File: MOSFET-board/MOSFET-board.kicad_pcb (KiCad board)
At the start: 2 copper layers, 76.2 x 76.2 mm, 104 parts, among them J1 PCIE-LP-01-01-F-DV-A-TR, J2 DB25_Female, U1 BTS3080EJXUMA1, U10 BTS3080EJXUMA1, U11 PCF8575_Breakout, U2 BTS3080EJXUMA1, U3 BTS3080EJXUMA1, U4 BTS3080EJXUMA1, U5 BTS3080EJXUMA1, U6 BTS3080EJXUMA1, U7 BTS3080EJXUMA1, U8 BTS3080EJXUMA1, U9 BTS3080EJXUMA1

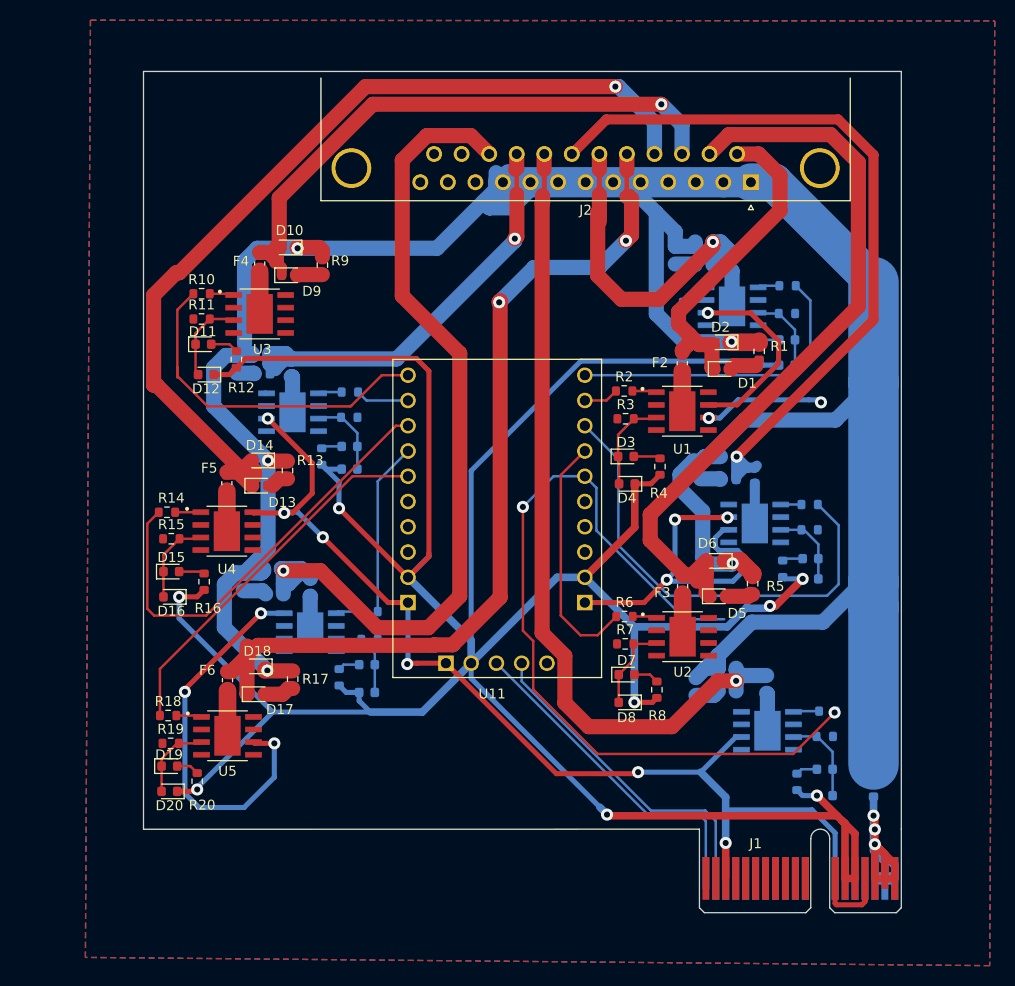
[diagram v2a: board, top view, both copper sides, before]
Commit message: Finished mosfet layout
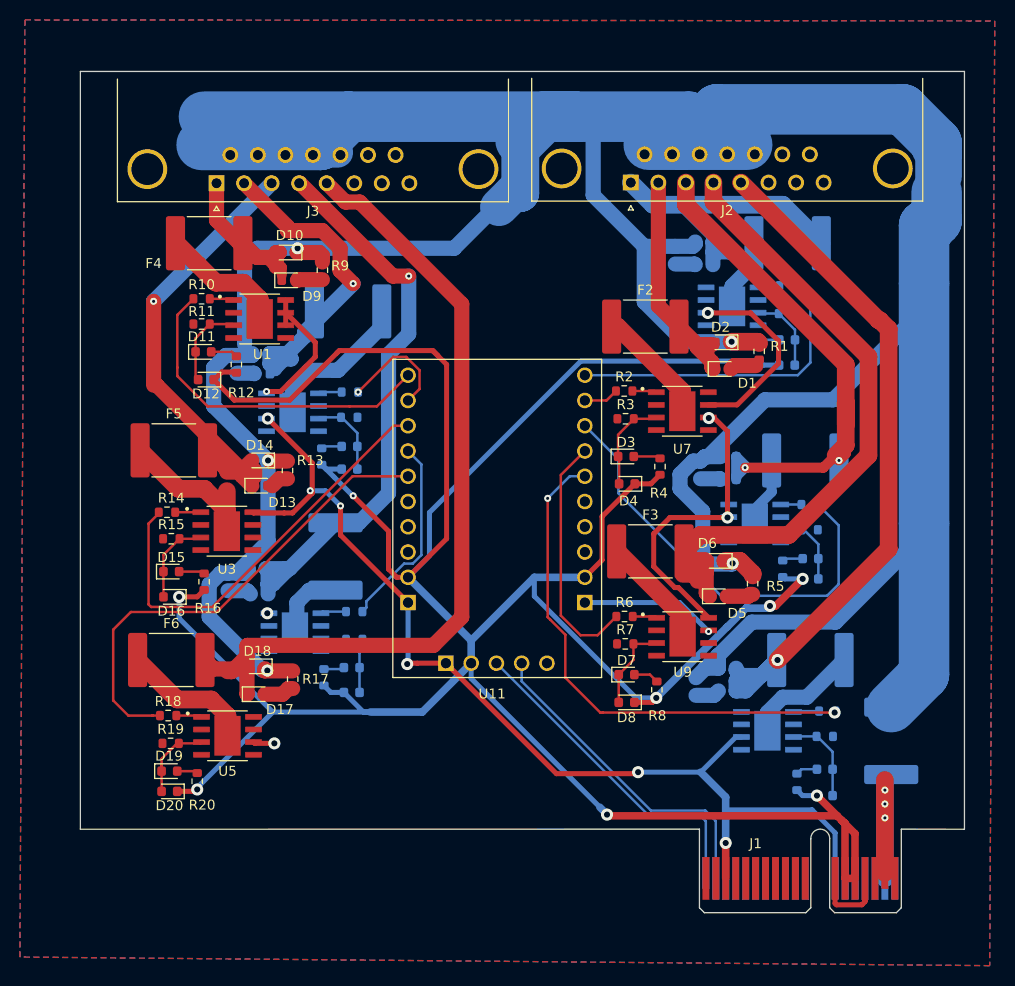
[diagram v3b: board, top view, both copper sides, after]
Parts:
- added J3: DB15_Female, Connector_Dsub:DSUB-15_Female_Horizontal_P2.77x2.84mm_EdgePinOffset7.70mm_Housed_MountingHolesOffset9.12mm, F.Cu at (134.3, 74.7)
- F1, F10, F11, F2, F3, F4, F5, F6, F7, F8, F9: footprint Fuse:Fuse_0603_1608Metric -> Fuse:Fuse_2920_7451Metric
- J2: value DB25_Female -> DB15_Female; footprint Connector_Dsub:DSUB-25_Male_Horizontal_P2.77x2.84mm_EdgePinOffset7.70mm_Housed_MountingHolesOffset9.12mm -> Connector_Dsub:DSUB-15_Female_Horizontal_P2.77x2.84mm_EdgePinOffset7.70mm_Housed_MountingHolesOffset9.12mm
- moved J2 12.1 mm to (176.0, 74.7)
- moved F10 7.99 mm to (147.6, 87.6), turned to 180 degrees
- moved F5 6.27 mm to (130.0, 101.6), turned to 0 degrees
- moved F6 6.01 mm to (129.8, 122.7), turned to 0 degrees
- moved F7 5.92 mm to (191.8, 80.8), turned to 0 degrees
- moved F4 5.47 mm to (133.6, 80.8), turned to 0 degrees
- moved F8 5.30 mm to (193.5, 102.6), turned to 0 degrees
- moved F2 5.23 mm to (177.5, 89.2), turned to 0 degrees
- moved F1 5.14 mm to (202.2, 130.8)
- moved F9 4.98 mm to (194.1, 122.7), turned to 180 degrees
- moved F3 4.77 mm to (178.0, 111.8), turned to 0 degrees
- moved F11 3.93 mm to (146.3, 112.3)
- moved D39 1.56 mm to (147.9, 123.4)
- moved D37 1.54 mm to (138.5, 116.0)
- moved D38 1.54 mm to (138.5, 113.5)
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- renumbered U3 to U1, U8 to U10, U9 to U2, U4 to U3, U10 to U4, U1 to U7, U7 to U8, U2 to U9
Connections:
- D1 pad 1: PYRO1 -> PYRO7
- D10 pad 2: PYRO3 -> PYRO1
- D13 pad 1: PYRO4 -> PYRO3
- D14 pad 2: PYRO4 -> PYRO3
- D2 pad 2: PYRO1 -> PYRO7
- D25 pad 1: PYRO7 -> PYRO8
- D26 pad 2: PYRO7 -> PYRO8
- D29 pad 1: PYRO8 -> PYRO10
- D30 pad 2: PYRO8 -> PYRO10
- D33 pad 1: PYRO9 -> PYRO2
- D34 pad 2: PYRO9 -> PYRO2
- D37 pad 1: PYRO10 -> PYRO4
- D38 pad 2: PYRO10 -> PYRO4
- D5 pad 1: PYRO2 -> PYRO9
- D6 pad 2: PYRO2 -> PYRO9
- D9 pad 1: PYRO3 -> PYRO1
- F10 pad 2: PYRO9 -> PYRO2
- F11 pad 2: PYRO10 -> PYRO4
- F2 pad 2: PYRO1 -> PYRO7
- F3 pad 2: PYRO2 -> PYRO9
- F4 pad 2: PYRO3 -> PYRO1
- F5 pad 2: PYRO4 -> PYRO3
- F8 pad 2: PYRO7 -> PYRO8
- F9 pad 2: PYRO8 -> PYRO10
- J2 pad 1: +12V -> PYRO6
- J2 pad 11: unconnected-(J2-Pad11) -> +12V
- J2 pad 12: unconnected-(J2-Pad12) -> +12V
- J2 pad 13: unconnected-(J2-Pad13) -> +12V
- J2 pad 14: PYRO1 -> unconnected-(J2-Pad14)
- J2 pad 15: PYRO2 -> unconnected-(J2-Pad15)
- J2 pad 2: +12V -> PYRO7
- J2 pad 3: +12V -> PYRO8
- J2 pad 4: +12V -> PYRO9
- J2 pad 5: +12V -> PYRO10
- J2 pad 6: +12V -> unconnected-(J2-Pad6)
- J2 pad 7: +12V -> unconnected-(J2-Pad7)
- J2 pad 8: +12V -> unconnected-(J2-Pad8)
- R10 pad 1: PYRO3EN -> PYRO1EN
- R11 pad 1: /Pyro 3/Status -> /Pyro 1/Status
- R14 pad 1: PYRO4EN -> PYRO3EN
- R15 pad 1: /Pyro 4/Status -> /Pyro 3/Status
- R2 pad 1: PYRO1EN -> PYRO7EN
- R26 pad 1: PYRO7EN -> PYRO8EN
- R27 pad 1: /Pyro 7/Status -> /Pyro 8/Status
- R3 pad 1: /Pyro 1/Status -> /Pyro 7/Status
- R30 pad 1: PYRO8EN -> PYRO10EN
- R31 pad 1: /Pyro 8/Status -> /Pyro 10/Status
- R34 pad 1: PYRO9EN -> PYRO2EN
- R35 pad 1: /Pyro 9/Status -> /Pyro 2/Status
- R38 pad 1: PYRO10EN -> PYRO4EN
- R39 pad 1: /Pyro 10/Status -> /Pyro 4/Status
- R6 pad 1: PYRO2EN -> PYRO9EN
- R7 pad 1: /Pyro 2/Status -> /Pyro 9/Status
- U11 pad 1: PYRO3EN -> PYRO1EN
- U11 pad 2: PYRO9EN -> PYRO2EN
- U11 pad 21: PYRO8EN -> PYRO10EN
- U11 pad 22: PYRO2EN -> PYRO9EN
- U11 pad 23: PYRO7EN -> PYRO8EN
- U11 pad 24: PYRO1EN -> PYRO7EN
- U11 pad 3: PYRO4EN -> PYRO3EN
- U11 pad 4: PYRO10EN -> PYRO4EN
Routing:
- net +12V: track 296.7 -> 397.4 mm
- net PYRO7: track 75.7 -> 24.7 mm, vias 1 -> 0
- net PYRO7EN: track 47.0 -> 3.53 mm
- net PYRO2: track 76.2 -> 35.4 mm, vias 0 -> 1
- net PYRO8EN: track 83.7 -> 44.0 mm, vias 2 -> 0
- net PYRO10EN: track 17.4 -> 52.1 mm, vias 0 -> 2
- net PYRO4: track 92.8 -> 58.2 mm
- net PYRO1EN: track 3.53 -> 34.2 mm
- net GND: track 226.0 -> 197.6 mm, vias 15 -> 13
- net PYRO8: track 83.9 -> 57.0 mm, vias 1 -> 2
- net PYRO4EN: track 44.6 -> 19.7 mm
- net PYRO9: track 44.7 -> 66.9 mm, vias 1 -> 0
- net PYRO9EN: track 5.37 -> 24.7 mm
- net PYRO1: track 33.2 -> 17.1 mm
- net PYRO10: track 86.8 -> 71.1 mm
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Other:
- board size 76.2 x 76.2 mm -> 88.9 x 76.2 mm

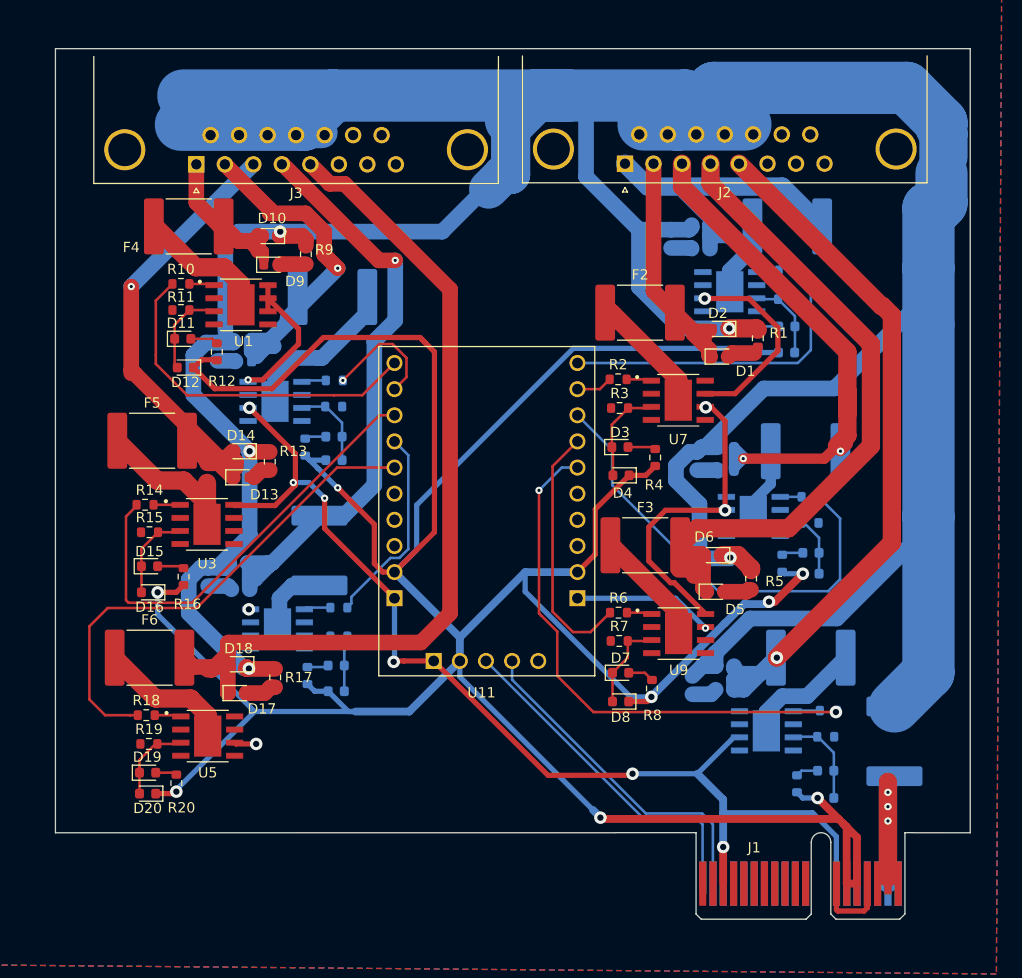
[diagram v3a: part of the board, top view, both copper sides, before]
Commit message: MOSFET Board Updated
MOSFET Board changes, new PCB Design and updated schematic.
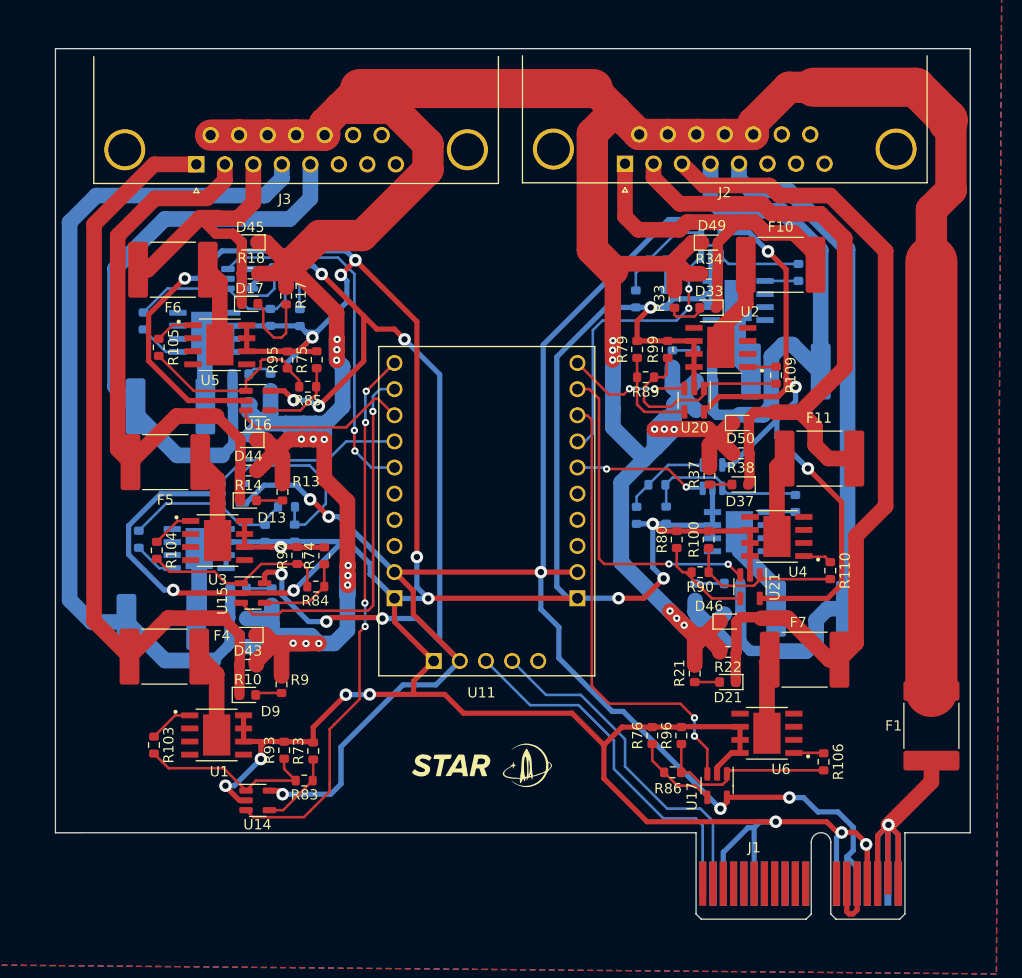
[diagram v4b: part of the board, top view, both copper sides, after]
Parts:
- removed D10, D12, D14, D16, D18, D2, D20, D22, D24, D26, D28, D30, D32, D34, D36, D38, D4, D40, D6, D8: D_Schottky, Diode_SMD:D_0603_1608Metric
- removed D11, D15, D19, D23, D27, D3, D31, D35, D39, D7: R_LED, LED_SMD:LED_0603_1608Metric
- removed R11, R15, R19, R23, R27, R3, R31, R35, R39, R7: 2k, Resistor_SMD:R_0603_1608Metric
- removed R12, R16, R20, R24, R28, R32, R36, R4, R40, R8: 3k, Resistor_SMD:R_0603_1608Metric
- added D41: D_Schottky, Diode_SMD:D_0603_1608Metric, B.Cu at (138.1, 121.6)
- added D42: D_Schottky, Diode_SMD:D_0603_1608Metric, B.Cu at (138.8, 101.0)
- added D43: D_Schottky, Diode_SMD:D_0603_1608Metric, F.Cu at (139.3, 120.5)
- added D44: D_Schottky, Diode_SMD:D_0603_1608Metric, F.Cu at (139.4, 101.5)
- added D45: D_Schottky, Diode_SMD:D_0603_1608Metric, F.Cu at (139.5, 82.3)
- added D46: D_Schottky, Diode_SMD:D_0603_1608Metric, F.Cu at (186.0, 119.2)
- added D47: D_Schottky, Diode_SMD:D_0603_1608Metric, B.Cu at (183.7, 98.6)
- added D48: D_Schottky, Diode_SMD:D_0603_1608Metric, B.Cu at (186.5, 121.1)
- added D49: D_Schottky, Diode_SMD:D_0603_1608Metric, F.Cu at (184.2, 82.3)
- added D50: D_Schottky, Diode_SMD:D_0603_1608Metric, F.Cu at (187.2, 99.9)
- added G***: LOGO, Symbol:STARLogo, F.Cu at (161.7, 133.1)
- added R100: 10k, Resistor_SMD:R_0603_1608Metric, F.Cu at (184.1, 111.2)
- added R101: 2k, Resistor_SMD:R_0603_1608Metric, B.Cu at (128.8, 111.2)
- added R102: 2k, Resistor_SMD:R_0603_1608Metric, B.Cu at (129.2, 90.0)
- added R103: 2k, Resistor_SMD:R_0603_1608Metric, F.Cu at (130.2, 131.2)
- added R104: 2k, Resistor_SMD:R_0603_1608Metric, F.Cu at (130.5, 112.2)
- added R105: 2k, Resistor_SMD:R_0603_1608Metric, F.Cu at (130.7, 92.5)
- added R106: 2k, Resistor_SMD:R_0603_1608Metric, F.Cu at (195.3, 132.8)
- added R107: 2k, Resistor_SMD:R_0603_1608Metric, B.Cu at (192.9, 85.2)
- added R108: 2k, Resistor_SMD:R_0603_1608Metric, B.Cu at (192.6, 107.7)
- added R109: 2k, Resistor_SMD:R_0603_1608Metric, F.Cu at (190.7, 95.2)
- added R110: 2k, Resistor_SMD:R_0603_1608Metric, F.Cu at (195.9, 114.2)
- added R71: 1k, Resistor_SMD:R_0603_1608Metric, B.Cu at (143.9, 110.6)
- added R72: 1k, Resistor_SMD:R_0603_1608Metric, B.Cu at (144.4, 89.6)
- added R73: 1k, Resistor_SMD:R_0603_1608Metric, F.Cu at (145.7, 131.8)
- added R74: 1k, Resistor_SMD:R_0603_1608Metric, F.Cu at (146.8, 112.8)
- added R75: 1k, Resistor_SMD:R_0603_1608Metric, F.Cu at (146.0, 93.7)
- added R76: 1k, Resistor_SMD:R_0603_1608Metric, F.Cu at (178.7, 130.2)
- added R77: 1k, Resistor_SMD:R_0603_1608Metric, B.Cu at (177.1, 87.8)
- added R78: 1k, Resistor_SMD:R_0603_1608Metric, B.Cu at (177.1, 108.8)
- added R79: 1k, Resistor_SMD:R_0603_1608Metric, F.Cu at (177.2, 92.7)
- added R80: 1k, Resistor_SMD:R_0603_1608Metric, F.Cu at (181.0, 111.2)
- added R81: 9k, Resistor_SMD:R_0603_1608Metric, B.Cu at (143.1, 108.0)
- added R82: 9k, Resistor_SMD:R_0603_1608Metric, B.Cu at (143.5, 86.1)
- added R83: 9k, Resistor_SMD:R_0603_1608Metric, F.Cu at (144.8, 134.6)
- added R84: 9k, Resistor_SMD:R_0603_1608Metric, F.Cu at (145.9, 115.8)
- added R85: 9k, Resistor_SMD:R_0603_1608Metric, F.Cu at (145.2, 96.3)
- added R86: 9k, Resistor_SMD:R_0603_1608Metric, F.Cu at (180.6, 133.8)
- added R87: 9k, Resistor_SMD:R_0603_1608Metric, B.Cu at (179.1, 84.1)
- added R88: 9k, Resistor_SMD:R_0603_1608Metric, B.Cu at (179.1, 105.9)
- added R89: 9k, Resistor_SMD:R_0603_1608Metric, F.Cu at (178.0, 95.4)
- added R90: 9k, Resistor_SMD:R_0603_1608Metric, F.Cu at (183.3, 114.4)
- added R91: 10k, Resistor_SMD:R_0603_1608Metric, B.Cu at (141.0, 110.6)
- added R92: 10k, Resistor_SMD:R_0603_1608Metric, B.Cu at (141.5, 89.6)
- added R93: 10k, Resistor_SMD:R_0603_1608Metric, F.Cu at (142.9, 131.7)
- added R94: 10k, Resistor_SMD:R_0603_1608Metric, F.Cu at (144.2, 112.8)
- added R95: 10k, Resistor_SMD:R_0603_1608Metric, F.Cu at (143.2, 93.8)
- added R96: 10k, Resistor_SMD:R_0603_1608Metric, F.Cu at (181.5, 130.2)
- added R97: 10k, Resistor_SMD:R_0603_1608Metric, B.Cu at (179.9, 87.8)
- added R98: 10k, Resistor_SMD:R_0603_1608Metric, B.Cu at (180.0, 108.8)
- added R99: 10k, Resistor_SMD:R_0603_1608Metric, F.Cu at (180.2, 92.7)
- added U12: INA193, Package_TO_SOT_SMD:SOT-23-5, B.Cu at (137.7, 106.8)
- added U13: INA193, Package_TO_SOT_SMD:SOT-23-5, B.Cu at (138.6, 85.9)
- added U14: INA193, Package_TO_SOT_SMD:SOT-23-5, F.Cu at (140.3, 136.6)
- added U15: INA193, Package_TO_SOT_SMD:SOT-23-5, F.Cu at (139.8, 116.4)
- added U16: INA193, Package_TO_SOT_SMD:SOT-23-5, F.Cu at (140.3, 97.7)
- added U17: INA193, Package_TO_SOT_SMD:SOT-23-5, F.Cu at (184.9, 135.1)
- added U18: INA193, Package_TO_SOT_SMD:SOT-23-5, B.Cu at (184.4, 82.5)
- added U19: INA193, Package_TO_SOT_SMD:SOT-23-5, B.Cu at (184.5, 105.1)
- added U20: INA193, Package_TO_SOT_SMD:SOT-23-5, F.Cu at (182.7, 97.7)
- added U21: INA193, Package_TO_SOT_SMD:SOT-23-5, F.Cu at (188.2, 115.8)
- D1, D5, F2, F3, U7, U9: moved to B.Cu
- D21, D33, D37, F1, F10, F11, F7, U2, U4, U6: moved to F.Cu
- R1, R5: value 3k -> 100; moved to B.Cu
- R10, R14, R18, R26, R30: value 2k -> 10k
- R13, R17, R25, R29, R9: value 3k -> 100
- R2, R6: value 2k -> 10k; moved to B.Cu
- R21, R33, R37: value 3k -> 100; moved to F.Cu
- R22, R34, R38: value 2k -> 10k; moved to F.Cu
- moved F2 55.4 mm to (130.9, 119.2), turned to 180 degrees
- moved U9 54.6 mm to (135.2, 91.1)
- moved R1 53.5 mm to (141.7, 116.8), turned to 90 degrees
- moved D1 52.0 mm to (138.4, 116.0)
- moved D5 50.7 mm to (138.7, 95.1)
- moved R5 50.5 mm to (141.6, 95.9), turned to 90 degrees
- moved D37 49.7 mm to (187.2, 105.8)
- moved R37 49.7 mm to (184.2, 105.0)
- moved F11 49.4 mm to (194.9, 103.3), turned to 0 degrees
- moved U4 49.4 mm to (190.8, 110.9)
- moved U7 48.7 mm to (134.6, 112.1)
- moved F3 48.1 mm to (131.8, 98.3), turned to 180 degrees
- moved D33 45.4 mm to (184.1, 88.7)
- moved R33 44.7 mm to (180.8, 87.8)
- moved R18 44.1 mm to (139.6, 85.3), turned to 180 degrees
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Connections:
- J1 pad A13: unconnected-(J1-PadA13) -> +5V
- J1 pad A14: unconnected-(J1-PadA14) -> +5V
- J2 pad 1: PYRO6 -> PYRO2
- J2 pad 2: PYRO7 -> PYRO4
- J2 pad 3: PYRO8 -> PYRO6
- J2 pad 4: PYRO9 -> PYRO8
- J3 pad 2: PYRO2 -> PYRO3
- J3 pad 3: PYRO3 -> PYRO5
- J3 pad 4: PYRO4 -> PYRO7
- J3 pad 5: PYRO5 -> PYRO9
- R10 pad 1: PYRO1EN -> +12V
- R10 pad 2: Net-(R10-Pad2) -> PYRO1
- R14 pad 1: PYRO3EN -> +12V
- R14 pad 2: Net-(R14-Pad2) -> PYRO3
- R18 pad 1: PYRO5EN -> +12V
- R18 pad 2: Net-(R18-Pad2) -> PYRO5
- R2 pad 1: PYRO7EN -> +12V
- R2 pad 2: Net-(R2-Pad2) -> PYRO7
- R22 pad 1: PYRO6EN -> +12V
- R22 pad 2: Net-(R22-Pad2) -> PYRO6
- R26 pad 1: PYRO8EN -> +12V
- R26 pad 2: Net-(R26-Pad2) -> PYRO8
- R30 pad 1: PYRO10EN -> +12V
- R30 pad 2: Net-(R30-Pad2) -> PYRO10
- R34 pad 1: PYRO2EN -> +12V
- R34 pad 2: Net-(R34-Pad2) -> PYRO2
- R38 pad 1: PYRO4EN -> +12V
- R38 pad 2: Net-(R38-Pad2) -> PYRO4
- R6 pad 1: PYRO9EN -> +12V
- R6 pad 2: Net-(R6-Pad2) -> PYRO9
- U1 pad 1: Net-(R10-Pad2) -> Net-(U1-IN)
- U1 pad 3: Net-(D11-Pad1) -> unconnected-(U1-STATUS-Pad3)
- U10 pad 1: Net-(R30-Pad2) -> Net-(U10-IN)
- U10 pad 3: Net-(D31-Pad1) -> unconnected-(U10-STATUS-Pad3)
- U11 pad 12: +3.3V -> +5V
- U11 pad 17: +3.3V -> +5V
- U11 pad 2: PYRO2EN -> PYRO3EN
- U11 pad 22: PYRO9EN -> PYRO8EN
- U11 pad 23: PYRO8EN -> PYRO6EN
- U11 pad 24: PYRO7EN -> PYRO4EN
- U11 pad 25: PYRO6EN -> PYRO2EN
- U11 pad 3: PYRO3EN -> PYRO5EN
- U11 pad 4: PYRO4EN -> PYRO7EN
- U11 pad 5: PYRO5EN -> PYRO9EN
- U11 pad 9: +3.3V -> +5V
- U2 pad 1: Net-(R34-Pad2) -> Net-(U2-IN)
- U2 pad 3: Net-(D35-Pad1) -> unconnected-(U2-STATUS-Pad3)
- U3 pad 1: Net-(R14-Pad2) -> Net-(U3-IN)
- U3 pad 3: Net-(D15-Pad1) -> unconnected-(U3-STATUS-Pad3)
- U4 pad 1: Net-(R38-Pad2) -> Net-(U4-IN)
- U4 pad 3: Net-(D39-Pad1) -> unconnected-(U4-STATUS-Pad3)
- U5 pad 1: Net-(R18-Pad2) -> Net-(U5-IN)
- U5 pad 3: Net-(D19-Pad1) -> unconnected-(U5-STATUS-Pad3)
- U6 pad 1: Net-(R22-Pad2) -> Net-(U6-IN)
- U6 pad 3: Net-(D23-Pad1) -> unconnected-(U6-STATUS-Pad3)
- U7 pad 1: Net-(R2-Pad2) -> Net-(U7-IN)
- U7 pad 3: Net-(D3-Pad1) -> unconnected-(U7-STATUS-Pad3)
- U8 pad 1: Net-(R26-Pad2) -> Net-(U8-IN)
- U8 pad 3: Net-(D27-Pad1) -> unconnected-(U8-STATUS-Pad3)
- U9 pad 1: Net-(R6-Pad2) -> Net-(U9-IN)
- U9 pad 3: Net-(D7-Pad1) -> unconnected-(U9-STATUS-Pad3)
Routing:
- net +5V: track 0.00 -> 332.0 mm, vias 0 -> 16
- net +3.3V: track 324.8 -> 6.54 mm, vias 8 -> 0
- net GND: track 197.6 -> 449.1 mm, vias 13 -> 20
- net +12V: track 397.4 -> 457.7 mm, vias 5 -> 21
- net PYRO7: track 24.7 -> 84.6 mm
- net PYRO1: track 17.1 -> 74.6 mm
- net PYRO5: track 84.9 -> 28.7 mm
- net PYRO6: track 37.9 -> 82.7 mm
- net PYRO10EN: track 52.1 -> 13.0 mm
- net PYRO5EN: track 48.5 -> 17.4 mm
- net Net-(F1-Pad1): track 20.1 -> 43.4 mm, vias 3 -> 1
- net Net-(R109-Pad2): track 0.00 -> 20.1 mm
- net PYRO1EN: track 34.2 -> 53.7 mm, vias 0 -> 4
- net Net-(R105-Pad2): track 0.00 -> 19.0 mm
- net Net-(R104-Pad2): track 0.00 -> 18.3 mm
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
